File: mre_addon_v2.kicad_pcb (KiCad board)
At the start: 2 copper layers, 76.6 x 46.8 mm, 92 parts, among them J1 TC2030, J10 Molex_Micro-Fit_3.0_43045-080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, J15 microSD_HC_Wuerth_693072010801, J15x MICRO-SDCARD-CONNECTOR-330006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, J2 Conn_01x06_Male, J20 Conn_02x05_Odd_Even-Connector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, J21 Soldering PAD for 12V_MREL, J3 Conn_01x03_Male, J30 Conn_02x05_Odd_Even-Connector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, J41 CONN_Sparkfun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

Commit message: V2.5 with OPAmp
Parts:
- removed the R17 at (127.7, 147.4)
- removed SW1: SW_Push, rusefi_lib:SW_SPST_CK_RS282G05A3
- added BOOT_TP1: TestPoint_2Pole, TestPoint:TestPoint_Bridge_Pitch2.54mm_Drill0.7mm, F.Cu at (79.2, 147.7)
- added J40: Molex_Micro-Fit_3.0_43045-0200_2x01_P3.00mm_Horizontal, Connector_Molex:Molex_Micro-Fit_3.0_43045-0212_2x01_P3.00mm_Vertical, F.Cu at (86.5, 130.1)
- added J40: Molex_Micro-Fit_3.0_43045-0200_2x01_P3.00mm_Horizontal, Connector_Molex:Molex_Micro-Fit_3.0_43045-0200_2x01_P3.00mm_Horizontal, F.Cu at (86.5, 130.1)
- added R35: 160k, Resistor_SMD:R_0603_1608Metric, F.Cu at (99.8, 135.4)
- added R36: 82k, Resistor_SMD:R_0603_1608Metric, F.Cu at (99.8, 138.4)
- added R37: 330, Resistor_SMD:R_0603_1608Metric, F.Cu at (97.2, 132.4)
- added R38: 10k, Resistor_SMD:R_0603_1608Metric, F.Cu at (94.2, 132.4)
- added R39: DNP (10k), Resistor_SMD:R_0603_1608Metric, F.Cu at (95.7, 132.4)
- added R40: 160k, Resistor_SMD:R_0603_1608Metric, F.Cu at (86.2, 138.7)
- added R41: 0, Resistor_SMD:R_0603_1608Metric, F.Cu at (89.2, 138.7)
- added R42: 330, Resistor_SMD:R_0603_1608Metric, F.Cu at (90.0, 135.7)
- added R43: DNP (10k), Resistor_SMD:R_0603_1608Metric, F.Cu at (88.2, 135.7)
- added R44: 10k, Resistor_SMD:R_0603_1608Metric, F.Cu at (86.5, 135.7)
- added U7: MCP6002, Package_SO:SOIC-8_3.9x4.9mm_P1.27mm, F.Cu at (94.8, 136.7)
- F1: value R_Axial_DIN0207_L6.3mm_D2.5mm_P10.16mm_Horizontal -> Polyfuse 2A
- moved J3 16.1 mm to (78.9, 136.0)
- moved C21 13.8 mm to (78.0, 139.3), turned to 90 degrees
- moved C26 13.7 mm to (78.0, 143.8), turned to -90 degrees
- moved LOGO1 9.23 mm to (99.8, 165.4)
- moved U5 8.43 mm to (81.5, 141.6), turned to -90 degrees
- moved C16 3.49 mm to (100.0, 132.3), turned to 0 degrees
- moved C23 0.55 mm to (89.3, 141.4)
- moved C24 0.54 mm to (87.6, 141.4), turned to -90 degrees
- moved J1 0.35 mm to (96.9, 128.9) (x2)
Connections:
- U1 pad 14: unconnected-(U1-Pad14) -> DAC2
- U1 pad 15: unconnected-(U1-Pad15) -> DAC1
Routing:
- net GND: track 94.5 -> 71.3 mm
- net /mcu_adc_mre_wbo2_v2/Boot0: track 14.8 -> 37.3 mm, vias 2 -> 1
- net DAC2: track 0.00 -> 21.8 mm, vias 0 -> 2
- net +5V: track 147.8 -> 169.4 mm, vias 2 -> 3
- net DAC1: track 0.00 -> 16.9 mm
- net /mcu_adc_mre_wbo2_v2/UART_RX: track 10.0 -> 24.5 mm, vias 0 -> 1
- net /mcu_adc_mre_wbo2_v2/UART_TX: track 7.48 -> 21.3 mm, vias 0 -> 1
- net /can_fet_egt_sd_v2/DAC1_OUT: track 0.00 -> 13.6 mm, vias 0 -> 1
- net CAN_RX: track 15.4 -> 26.8 mm, vias 0 -> 2
- net Net-(R36-Pad2): track 0.00 -> 8.84 mm
- net /can_fet_egt_sd_v2/DAC2_OUT: track 0.00 -> 8.24 mm
- net Net-(R40-Pad2): track 0.00 -> 7.73 mm
- net +3.3V: track 255.6 -> 261.0 mm
- net Net-(R41-Pad2): track 0.00 -> 4.35 mm
- net Net-(R35-Pad2): track 0.00 -> 3.56 mm
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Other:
- rule pad_to_mask_clearance: 0.051 -> 0
- board text added: "MCP6002"

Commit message: V2.5 with OPAmp
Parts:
- moved C24 0.10 mm to (87.5, 141.4), turned to 90 degrees
- turned C26 to 90 degrees
- renumbered G*** to G1, U3x to U3
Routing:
- net /can_fet_egt_sd_v2/CAN_L: track 8.82 -> 9.69 mm
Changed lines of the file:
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@@
   )
   (footprint "Capacitor_SMD:C_0603_1608Metric" (layer "F.Cu")
-    (at 87.6 141.45 -90)
+    (at 87.5 141.45 90)
     (descr "Capacitor SMD 0603 (1608 Metric), square (rectangular) end terminal, IPC_7351 nominal, (Body size source: http://www.tortai-tech.com/upload/download/2011102023233369053.pdf), generated with kicad-footprint-generator")
     (tags "capacitor")
@@
     (property "Sheetname" "can_fet_egt_sd_v2")
     (attr smd)
-    (fp_text reference "C24" (at -1.75 0) (layer "F.SilkS")
+    (fp_text reference "C24" (at 1.75 0) (layer "F.SilkS")
       (effects (font (size 0.5 0.5) (thickness 0.125)))
     )
@@
     (fp_line (start -0.8 -0.4) (end 0.8 -0.4) (layer "F.Fab") (width 0.1))
     (fp_line (start 0.8 -0.4) (end 0.8 0.4) (layer "F.Fab") (width 0.1))
-    (pad "1" smd roundrect locked (at -0.7875 0 270) (size 0.875 0.95) (layers "F.Cu" "F.Paste" "F.Mask") (roundrect_rratio 0.25)
+    (pad "1" smd roundrect locked (at -0.7875 0 90) (size 0.875 0.95) (layers "F.Cu" "F.Paste" "F.Mask") (roundrect_rratio 0.25)
       (net 29 "/can_fet_egt_sd_v2/CAN_L") (pintype "passive"))
-    (pad "2" smd roundrect locked (at 0.7875 0 270) (size 0.875 0.95) (layers "F.Cu" "F.Paste" "F.Mask") (roundrect_rratio 0.25)
+    (pad "2" smd roundrect locked (at 0.7875 0 90) (size 0.875 0.95) (layers "F.Cu" "F.Paste" "F.Mask") (roundrect_rratio 0.25)
       (net 1 "GND") (pintype "passive") (zone_connect 2))
     (model "${KISYS3DMOD}/Capacitor_SMD.3dshapes/C_0603_1608Metric.wrl"
@@
     (at 95.493844 153.712278)
     (attr through_hole)
-    (fp_text reference "G***" (at 0 0 180) (layer "F.SilkS") hide
+    (fp_text reference "G1" (at 0 0 180) (layer "F.SilkS") hide
       (effects (font (size 1.524 1.524) (thickness 0.3)))
     )
@@
   )
   (footprint "Capacitor_SMD:C_0603_1608Metric" (layer "F.Cu")
-    (at 77.95 143.75 -90)
+    (at 77.95 143.75 90)
     (descr "Capacitor SMD 0603 (1608 Metric), square (rectangular) end terminal, IPC_7351 nominal, (Body size source: http://www.tortai-tech.com/upload/download/2011102023233369053.pdf), generated with kicad-footprint-generator")
     (tags "capacitor")
@@
     (fp_line (start 0.8 0.4) (end -0.8 0.4) (layer "F.Fab") (width 0.1))
     (fp_line (start -0.8 -0.4) (end 0.8 -0.4) (layer "F.Fab") (width 0.1))
-    (pad "1" smd roundrect locked (at -0.7875 0 270) (size 0.875 0.95) (layers "F.Cu" "F.Paste" "F.Mask") (roundrect_rratio 0.25)
+    (pad "1" smd roundrect locked (at -0.7875 0 90) (size 0.875 0.95) (layers "F.Cu" "F.Paste" "F.Mask") (roundrect_rratio 0.25)
       (net 8 "+3.3V") (pintype "passive"))
-    (pad "2" smd roundrect locked (at 0.7875 0 270) (size 0.875 0.95) (layers "F.Cu" "F.Paste" "F.Mask") (roundrect_rratio 0.25)
+    (pad "2" smd roundrect locked (at 0.7875 0 90) (size 0.875 0.95) (layers "F.Cu" "F.Paste" "F.Mask") (roundrect_rratio 0.25)
       (net 1 "GND") (pintype "passive") (zone_connect 2))
     (model "${KISYS3DMOD}/Capacitor_SMD.3dshapes/C_0603_1608Metric.wrl"
@@
     (tags "SO SO")
     (attr smd)
-    (fp_text reference "U3x" (at 0 -3.4) (layer "F.SilkS") hide
+    (fp_text reference "U3" (at 0 -3.4) (layer "F.SilkS") hide
       (effects (font (size 1 1) (thickness 0.15)))
     )
@@
       (net 8 "+3.3V") (pinfunction "1") (pintype "passive"))
     (pad "2" thru_hole circle (at 2.54 0) (size 1.4 1.4) (drill 0.7) (layers *.Cu *.Mask)
-      (net 55 "/mcu_adc_mre_wbo2_v2/Boot0") (pinfunction "1") (pintype "passive"))
+      (net 55 "/mcu_adc_mre_wbo2_v2/Boot0") (pinfunction "2") (pintype "passive"))
     (model "${KICAD6_3DMODEL_DIR}/TestPoint.3dshapes/TestPoint_Bridge_Pitch2.54mm_Drill0.7mm.wrl"
       (offset (xyz 0 0 0))
@@
     (property "Sheetname" "mcu_adc_mre_wbo2_v2")
     (attr smd)
-    (fp_text reference "Y1" (at -0.05 -2.733335 180) (layer "F.SilkS")
+    (fp_text reference "Y1" (at -0.05 -2.783335 180) (layer "F.SilkS")
       (effects (font (size 1 1) (thickness 0.15)))
     )
@@
       (effects (font (size 0.75 0.75) (thickness 0.13)) (justify mirror))
     )
-    (fp_text user "CANH" (at 23.8293 5.6053 180) (layer "B.SilkS")
+    (fp_text user "CANH" (at 24.1906 6.4678 180) (layer "B.SilkS")
       (effects (font (size 0.75 0.75) (thickness 0.15)) (justify mirror))
     )
@@
       (effects (font (size 1 1) (thickness 0.15)) (justify mirror))
     )
-    (fp_text user "CANL" (at 29.5713 5.6053 180) (layer "B.SilkS")
+    (fp_text user "CANL" (at 29.9406 6.4678 180) (layer "B.SilkS")
       (effects (font (size 0.75 0.75) (thickness 0.15)) (justify mirror))
     )
@@
   (segment (start 135.8 155.65) (end 135.75 155.6) (width 0.25) (layer "F.Cu") (net 8))
   (segment (start 113.95 142.05) (end 113.94375 142.05625) (width 0.25) (layer "F.Cu") (net 8))
-  (segment (start 77.95 142.9625) (end 78.4125 142.5) (width 0.25) (layer "F.Cu") (net 8))
   (segment (start 95.655 129.5) (end 95.355 129.8) (width 0.25) (layer "F.Cu") (net 8))
   (segment (start 100.4 166.1975) (end 100.4 170.1) (width 0.3) (layer "F.Cu") (net 8))
   (segment (start 127.508 171.542) (end 127.508 169.6316) (width 0.3) (layer "F.Cu") (net 8))
+  (segment (start 77.95 144.5375) (end 79.0825 144.5375) (width 0.25) (layer "F.Cu") (net 8))
   (segment (start 127.3 171.75) (end 127.508 171.542) (width 0.3) (layer "F.Cu") (net 8))
-  (segment (start 78.4125 142.5) (end 79.6 142.5) (width 0.25) (layer "F.Cu") (net 8))
   (segment (start 93.958884 134.175) (end 94.325 134.541116) (width 0.25) (layer "F.Cu") (net 8))
   (segment (start 127.508 164.5816) (end 127.508 169.6316) (width 0.6) (layer "F.Cu") (net 8))
@@
   (segment (start 136.13 155.65) (end 135.8 155.65) (width 0.25) (layer "F.Cu") (net 8))
   (segment (start 93.9 138) (end 93.9 135.483884) (width 0.25) (layer "F.Cu") (net 8))
+  (segment (start 79.0825 144.5375) (end 79.595 144.025) (width 0.25) (layer "F.Cu") (net 8))
   (segment (start 108.4 138.4) (end 108.4 136.225) (width 0.25) (layer "F.Cu") (net 8))
   (segment (start 129.175 155.65) (end 135.8 155.65) (width 0.25) (layer "F.Cu") (net 8))
@@
   (segment (start 88.1512 143.4) (end 85.8 143.4) (width 0.25) (layer "F.Cu") (net 28))
   (segment (start 81.33 142.15) (end 81.355 142.175) (width 0.25) (layer "F.Cu") (net 29))
+  (segment (start 81.355 142.175) (end 85.375 142.175) (width 0.25) (layer "F.Cu") (net 29))
+  (segment (start 85.375 142.175) (end 87.5375 142.175) (width 0.25) (layer "F.Cu") (net 29))
   (segment (start 80.865 142.615) (end 80.865 144.025) (width 0.25) (layer "F.Cu") (net 29))
-  (segment (start 85.3606 140.7718) (end 87.4907 140.7718) (width 0.25) (layer "F.Cu") (net 29))
-  (segment (start 81.355 142.175) (end 83.9574 142.175) (width 0.25) (layer "F.Cu") (net 29))
-  (segment (start 83.9574 142.175) (end 85.3606 140.7718) (width 0.25) (layer "F.Cu") (net 29))
+  (segment (start 85.3606 140.7718) (end 85.3606 142.1606) (width 0.25) (layer "F.Cu") (net 29))
   (segment (start 80.865 142.615) (end 81.33 142.15) (width 0.25) (layer "F.Cu") (net 29))
+  (segment (start 85.3606 142.1606) (end 85.375 142.175) (width 0.25) (layer "F.Cu") (net 29))
   (segment (start 139.665 159.135) (end 144.915 153.885) (width 0.5) (layer "F.Cu") (net 30))
   (segment (start 144.915 153.885) (end 144.915 152.975) (width 0.5) (layer "F.Cu") (net 30))

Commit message: V2.5 with OPAmp
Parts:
- added C28: 100n, Capacitor_SMD:C_0603_1608Metric, F.Cu at (69.7, 133.3)
- added R45: 120, Resistor_SMD:R_0805_2012Metric, F.Cu at (65.4, 133.6)
- R40: value 160k -> 100k
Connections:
- R40 pad 2: Net-(R40-Pad2) -> Net-(R41-Pad1)
- R41 pad 1: Net-(R40-Pad2) -> Net-(R41-Pad1)
- U7 pad 5: DAC2 -> Net-(R41-Pad1)
- U7 pad 6: Net-(R40-Pad2) -> DAC2
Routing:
- net Net-(R41-Pad1): track 0.00 -> 8.04 mm
- net Net-(R40-Pad2): track 7.73 -> 0.00 mm
- net DAC2: track 21.8 -> 22.6 mm

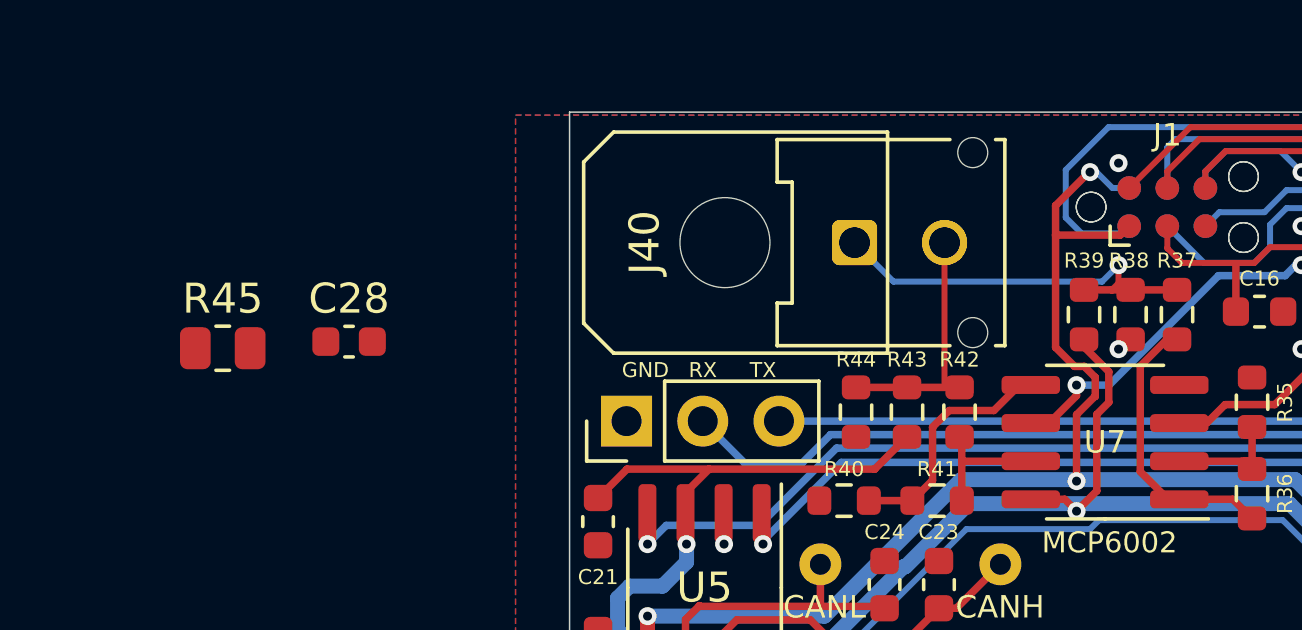
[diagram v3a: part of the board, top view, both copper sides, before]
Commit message: some changes on DAC pins
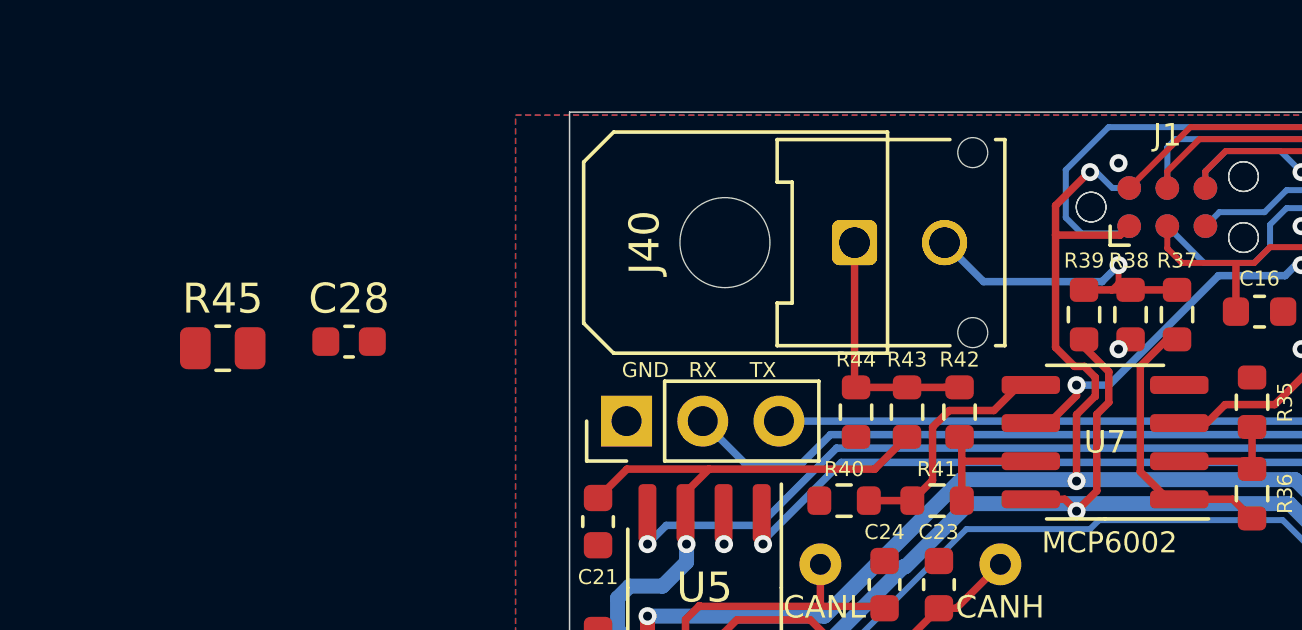
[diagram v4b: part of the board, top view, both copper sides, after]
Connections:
- R37 pad 2: /can_fet_egt_sd_v2/DAC1_OUT -> /can_fet_egt_sd_v2/DAC2_OUT
- R38 pad 1: /can_fet_egt_sd_v2/DAC1_OUT -> /can_fet_egt_sd_v2/DAC2_OUT
- R39 pad 2: /can_fet_egt_sd_v2/DAC1_OUT -> /can_fet_egt_sd_v2/DAC2_OUT
- R42 pad 2: /can_fet_egt_sd_v2/DAC2_OUT -> /can_fet_egt_sd_v2/DAC1_OUT
- R43 pad 1: /can_fet_egt_sd_v2/DAC2_OUT -> /can_fet_egt_sd_v2/DAC1_OUT
- R44 pad 2: /can_fet_egt_sd_v2/DAC2_OUT -> /can_fet_egt_sd_v2/DAC1_OUT
- U1 pad 14: DAC2 -> DAC1
- U1 pad 15: DAC1 -> DAC2
- U7 pad 3: DAC1 -> DAC2
- U7 pad 6: DAC2 -> DAC1
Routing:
- net DAC2: track 22.6 -> 16.9 mm, vias 2 -> 0
- net DAC1: track 16.9 -> 22.6 mm, vias 0 -> 2
- net /can_fet_egt_sd_v2/DAC1_OUT: track 13.6 -> 8.28 mm, vias 1 -> 0
- net /can_fet_egt_sd_v2/DAC2_OUT: track 8.24 -> 10.6 mm, vias 0 -> 1

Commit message: V2.5 - 13.02.2023
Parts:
- added PA15: TestPoint, TestPoint:TestPoint_Pad_D1.0mm, F.Cu at (103.0, 143.0)
- added PB0: TestPoint, TestPoint:TestPoint_Pad_D1.0mm, B.Cu at (112.0, 132.3)
- added PB10: TestPoint, TestPoint:TestPoint_Pad_D1.0mm, B.Cu at (109.9, 132.3)
- added PB11: TestPoint, TestPoint:TestPoint_Pad_D1.0mm, B.Cu at (107.8, 132.3)
- added PB12: TestPoint, TestPoint:TestPoint_Pad_D1.0mm, B.Cu at (104.1, 132.3)
- added PB13: TestPoint, TestPoint:TestPoint_Pad_D1.0mm, B.Cu at (102.0, 132.3)
- added PB14: TestPoint, TestPoint:TestPoint_Pad_D1.0mm, B.Cu at (100.2, 134.3)
- added PB15: TestPoint, TestPoint:TestPoint_Pad_D1.0mm, B.Cu at (98.0, 134.3)
- added PB3: TestPoint, TestPoint:TestPoint_Pad_D1.0mm, F.Cu at (105.2, 143.0)
- added PB4: TestPoint, TestPoint:TestPoint_Pad_D1.0mm, F.Cu at (107.2, 143.0)
- added PB8: TestPoint, TestPoint:TestPoint_Pad_D1.0mm, B.Cu at (110.5, 139.4)
- added PB9: TestPoint, TestPoint:TestPoint_Pad_D1.0mm, B.Cu at (112.5, 139.4)
- renumbered J30 to J30x, U3 to U3x
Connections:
- U1 pad 18: unconnected-(U1-Pad18) -> Net-(PB0-Pad1)
- U1 pad 21: unconnected-(U1-Pad21) -> Net-(PB10-Pad1)
- U1 pad 22: unconnected-(U1-Pad22) -> Net-(PB11-Pad1)
- U1 pad 25: unconnected-(U1-Pad25) -> Net-(PB12-Pad1)
- U1 pad 26: unconnected-(U1-Pad26) -> Net-(PB13-Pad1)
- U1 pad 27: unconnected-(U1-Pad27) -> Net-(PB14-Pad1)
- U1 pad 28: unconnected-(U1-Pad28) -> Net-(PB15-Pad1)
- U1 pad 38: unconnected-(U1-Pad38) -> Net-(PA15-Pad1)
- U1 pad 39: unconnected-(U1-Pad39) -> Net-(PB3-Pad1)
- U1 pad 40: unconnected-(U1-Pad40) -> Net-(PB4-Pad1)
- U1 pad 45: unconnected-(U1-Pad45) -> Net-(PB8-Pad1)
- U1 pad 46: unconnected-(U1-Pad46) -> Net-(PB9-Pad1)
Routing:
- net Net-(PB15-Pad1): track 0.00 -> 7.73 mm, vias 0 -> 1
- net Net-(PA15-Pad1): track 0.00 -> 5.14 mm
- net Net-(PB14-Pad1): track 0.00 -> 5.07 mm, vias 0 -> 1
- net Net-(PB0-Pad1): track 0.00 -> 4.68 mm, vias 0 -> 1
- net Net-(PB13-Pad1): track 0.00 -> 4.48 mm, vias 0 -> 1
- net Net-(PB10-Pad1): track 0.00 -> 3.79 mm, vias 0 -> 1
- net Net-(PB3-Pad1): track 0.00 -> 3.65 mm
- net Net-(PB12-Pad1): track 0.00 -> 3.04 mm, vias 0 -> 1
- net Net-(PB11-Pad1): track 0.00 -> 2.79 mm, vias 0 -> 1
- net Net-(PB9-Pad1): track 0.00 -> 2.63 mm, vias 0 -> 1
- net Net-(PB4-Pad1): track 0.00 -> 2.54 mm
- net /mcu_adc_mre_wbo2_v2/SWCLK: track 56.8 -> 59.1 mm
- net GND: track 71.3 -> 69.4 mm, vias 65 -> 64
- net /mcu_adc_mre_wbo2_v2/Ip_dac: track 22.7 -> 21.1 mm
- net Net-(PB8-Pad1): track 0.00 -> 1.48 mm, vias 0 -> 1
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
